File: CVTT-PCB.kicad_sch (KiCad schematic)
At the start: 66 parts, among them J1 SERVO1, J2 SERVO2, J3 LCD SCREEN, J4 LCD BUTTONS, J5 Conn_ARM_SWD_TagConnect_TC2030, J7 Barrel_Jack, P2 DC2, P5 DC1, P8 STEPPER, Q7 BSS138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

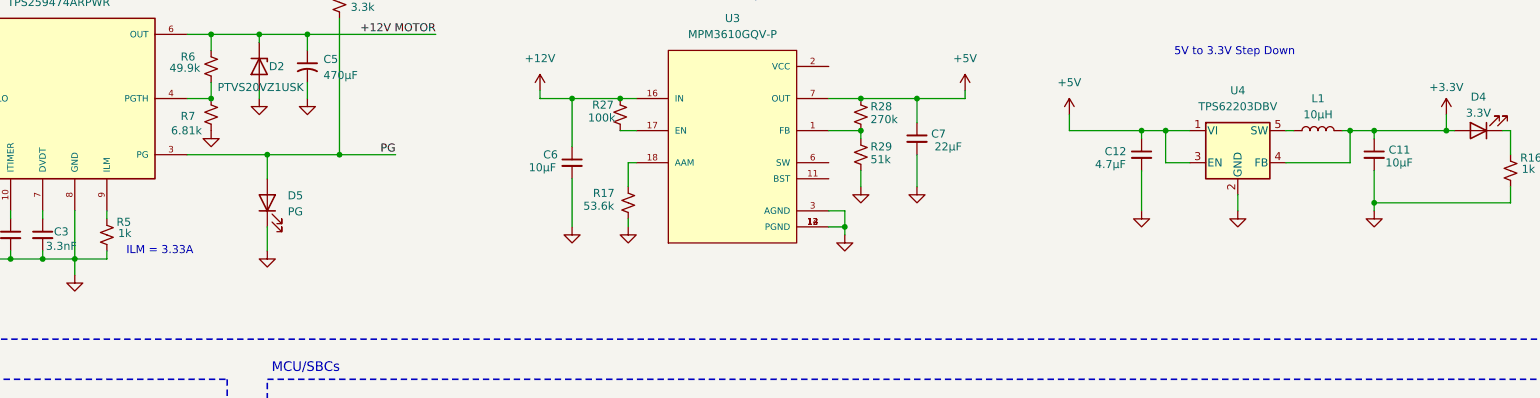
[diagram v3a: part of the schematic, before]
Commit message: reconfigure ILM for motor req
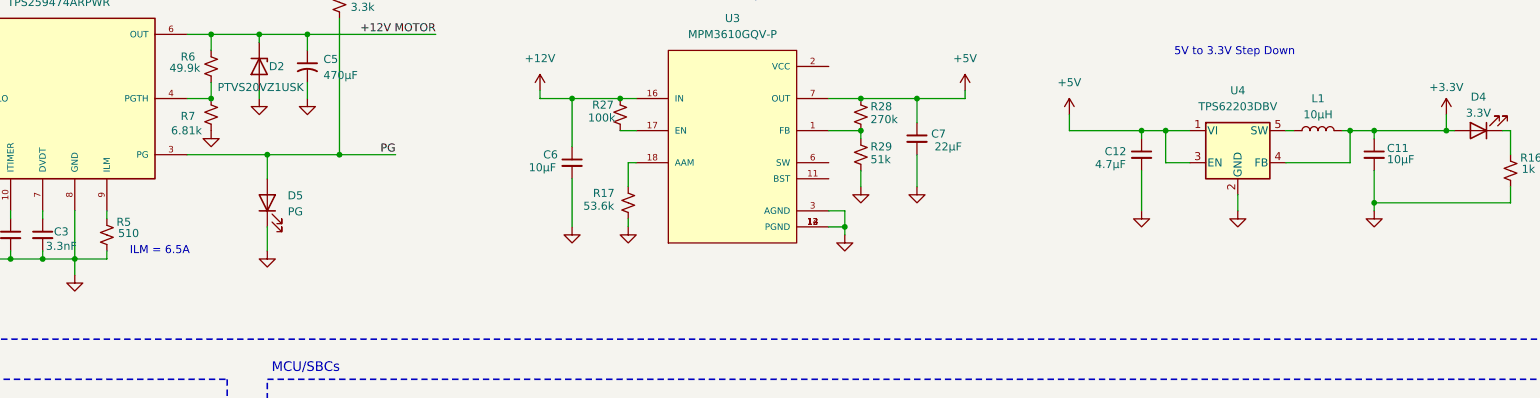
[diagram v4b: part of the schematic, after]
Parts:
- C11, C6: Manufacturer (none) -> Murata Electronics; Part Number (none) -> GRM188R61E106KA73D
- C12: Manufacturer (none) -> Samsung Electro-Mechanics; Part Number (none) -> CL10A475KO8NNNC
- C7: Manufacturer (none) -> Samsung Electro-Mechanics; Part Number (none) -> CL10A226MO7JZNC
- R17: Manufacturer (none) -> Vishay Dale; Part Number (none) -> CRCW060353K6FKEAC
- R5: value 1k -> 510; Manufacturer Vishay Dale -> YAGEO; Part Number RCS06031K00FKEA -> RC0603FR-07510RL
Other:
- note added: "ILM = 6.5A"
- note removed: "ILM = 3.33A"
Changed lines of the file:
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@@
 		)
 	)
-	(text "ILM = 3.33A"
+	(text "ILM = 6.5A"
 		(exclude_from_sim no)
 		(at 172.212 73.66 0)
@@
 			)
 		)
-		(property "Datasheet" ""
+		(property "Datasheet" "https://mm.digikey.com/Volume0/opasdata/d220001/medias/docus/2328/CL10A475KO8NNNC_Spec.pdf"
 			(at 327.66 58.42 0)
 			(effects
@@
 			)
 		)
-		(property "Description" ""
+		(property "Description" "CAP CER 4.7UF 16V X5R 0603"
 			(at 327.66 58.42 0)
 			(effects
@@
 			)
 		)
-		(property "Part Number" ""
+		(property "Part Number" "CL10A475KO8NNNC"
 			(at 327.66 58.42 0)
 			(effects
@@
 			)
 		)
-		(property "Manufacturer" ""
+		(property "Manufacturer" "Samsung Electro-Mechanics"
 			(at 327.66 58.42 0)
 			(effects
@@
 	)
 	(symbol
-		(lib_id "Device:C_Small")
-		(at 364.49 58.42 0)
-		(unit 1)
-		(exclude_from_sim no)
-		(in_bom yes)
-		(on_board yes)
-		(dnp no)
-		(property "Reference" "C11"
-			(at 366.776 57.658 0)
-			(effects
-				(font
-					(size 1.27 1.27)
-				)
-				(justify left)
-			)
-		)
-		(property "Value" "10µF"
-			(at 366.268 59.69 0)
-			(effects
-				(font
-					(size 1.27 1.27)
-				)
-				(justify left)
-			)
-		)
-		(property "Footprint" "Capacitor_SMD:C_0603_1608Metric_Pad1.08x0.95mm_HandSolder"
-			(at 364.49 58.42 0)
-			(effects
-				(font
-					(size 1.27 1.27)
-				)
-				(hide yes)
-			)
-		)
-		(property "Datasheet" ""
-			(at 364.49 58.42 0)
-			(effects
-				(font
-					(size 1.27 1.27)
-				)
-				(hide yes)
-			)
-		)
-		(property "Description" ""
-			(at 364.49 58.42 0)
-			(effects
-				(font
-					(size 1.27 1.27)
-				)
-				(hide yes)
-			)
-		)
-		(property "Part Number" ""
-			(at 364.49 58.42 0)
-			(effects
-				(font
-					(size 1.27 1.27)
-				)
-				(hide yes)
-			)
-		)
-		(property "Manufacturer" ""
-			(at 364.49 58.42 0)
-			(effects
-				(font
-					(size 1.27 1.27)
-				)
-				(hide yes)
-			)
-		)
-		(pin "1"
-		)
-		(pin "2"
-		)
-		(instances
-			(project "CVTT-PCB"
-				(path "/1cfd431a-19b0-4ea1-8526-1e2a0b724830"
-					(reference "C11")
-					(unit 1)
-				)
-			)
-		)
-	)
-	(symbol
 		(lib_id "power:+3.3V")
 		(at 71.12 115.57 0)
@@
 			)
 		)
-		(property "Datasheet" ""
+		(property "Datasheet" "https://mm.digikey.com/Volume0/opasdata/d220001/medias/docus/2139/CL10A226MO7JZNC_Spec.pdf"
 			(at 292.1 55.88 0)
 			(effects
@@
 			)
 		)
-		(property "Description" ""
+		(property "Description" "CAP CER 22UF 16V X5R 0603"
 			(at 292.1 55.88 0)
 			(effects
@@
 			)
 		)
-		(property "Part Number" ""
+		(property "Part Number" "CL10A226MO7JZNC"
 			(at 292.1 55.88 0)
 			(effects
@@
 			)
 		)
-		(property "Manufacturer" ""
+		(property "Manufacturer" "Samsung Electro-Mechanics"
 			(at 292.1 55.88 0)
 			(effects
@@
 			)
 		)
-		(property "Datasheet" ""
+		(property "Datasheet" "https://www.vishay.com/docs/28773/crcwce3.pdf"
 			(at 246.38 66.04 0)
 			(effects
@@
 			)
 		)
-		(property "Description" ""
+		(property "Description" "RES 53.6K OHM 1% 1/10W 0603"
 			(at 246.38 66.04 0)
 			(effects
@@
 			)
 		)
-		(property "Part Number" ""
+		(property "Part Number" "CRCW060353K6FKEAC"
 			(at 246.38 66.04 0)
 			(effects
@@
 			)
 		)
-		(property "Manufacturer" ""
+		(property "Manufacturer" "Vishay Dale"
 			(at 246.38 66.04 0)
 			(effects
@@
 			)
 		)
-		(property "Value" "1k"
+		(property "Value" "510"
 			(at 165.608 70.866 0)
 			(effects
@@
 			)
 		)
-		(property "Datasheet" "https://www.vishay.com/docs/20065/rcse3.pdf"
+		(property "Datasheet" "https://www.yageo.com/upload/media/product/products/datasheet/rchip/PYu-RC_Group_51_RoHS_L_12.pdf"
 			(at 163.83 71.12 0)
 			(effects
@@
 			)
 		)
-		(property "Description" "RES SMD 1K OHM 1% 1/4W 0603"
+		(property "Description" "RES 510 OHM 1% 1/10W 0603"
 			(at 163.83 71.12 0)
 			(effects
@@
 			)
 		)
-		(property "Part Number" "RCS06031K00FKEA"
+		(property "Part Number" "RC0603FR-07510RL"
 			(at 163.83 71.12 0)
 			(effects
@@
 			)
 		)
-		(property "Manufacturer" "Vishay Dale"
+		(property "Manufacturer" "YAGEO"
 			(at 163.83 71.12 0)
 			(effects
@@
 	)
 	(symbol
+		(lib_id "Device:C_Small")
+		(at 364.49 58.42 0)
+		(unit 1)
+		(exclude_from_sim no)
+		(in_bom yes)
+		(on_board yes)
+		(dnp no)
+		(property "Reference" "C11"
+			(at 366.522 57.404 0)
+			(effects
+				(font
+					(size 1.27 1.27)
+				)
+				(justify left)
+			)
+		)
+		(property "Value" "10µF"
+			(at 366.522 59.182 0)
+			(effects
+				(font
+					(size 1.27 1.27)
+				)
+				(justify left)
+			)
+		)
+		(property "Footprint" "Capacitor_SMD:C_0603_1608Metric_Pad1.08x0.95mm_HandSolder"
+			(at 364.49 58.42 0)
+			(effects
+				(font
+					(size 1.27 1.27)
+				)
+				(hide yes)
+			)
+		)
+		(property "Datasheet" "https://search.murata.co.jp/Ceramy/image/img/A01X/G101/ENG/GRM188R61E106KA73-01.pdf"
+			(at 364.49 58.42 0)
+			(effects
+				(font
+					(size 1.27 1.27)
+				)
+				(hide yes)
+			)
+		)
+		(property "Description" "CAP CER 10UF 25V X5R 0603"
+			(at 364.49 58.42 0)
+			(effects
+				(font
+					(size 1.27 1.27)
+				)
+				(hide yes)
+			)
+		)
+		(property "Part Number" "GRM188R61E106KA73D"
+			(at 364.49 58.42 0)
+			(effects
+				(font
+					(size 1.27 1.27)
+				)
+				(hide yes)
+			)
+		)
+		(property "Manufacturer" "Murata Electronics"
+			(at 364.49 58.42 0)
+			(effects
+				(font
+					(size 1.27 1.27)
+				)
+				(hide yes)
+			)
+		)
+		(pin "1"
+		)
+		(pin "2"
+		)
+		(instances
+			(project "CVTT-PCB"
+				(path "/1cfd431a-19b0-4ea1-8526-1e2a0b724830"
+					(reference "C11")
+					(unit 1)
+				)
+			)
+		)
+	)
+	(symbol
 		(lib_id "power:+5V")
 		(at 316.23 52.07 0)
@@
 			)
 		)
-		(property "Datasheet" ""
+		(property "Datasheet" "https://search.murata.co.jp/Ceramy/image/img/A01X/G101/ENG/GRM188R61E106KA73-01.pdf"
 			(at 237.49 59.69 0)
 			(effects
@@
 			)
 		)
-		(property "Description" ""
+		(property "Description" "CAP CER 10UF 25V X5R 0603"
 			(at 237.49 59.69 0)
 			(effects
@@
 			)
 		)
-		(property "Part Number" ""
+		(property "Part Number" "GRM188R61E106KA73D"
 			(at 237.49 59.69 0)
 			(effects
@@
 			)
 		)
-		(property "Manufacturer" ""
+		(property "Manufacturer" "Murata Electronics"
 			(at 237.49 59.69 0)
 			(effects

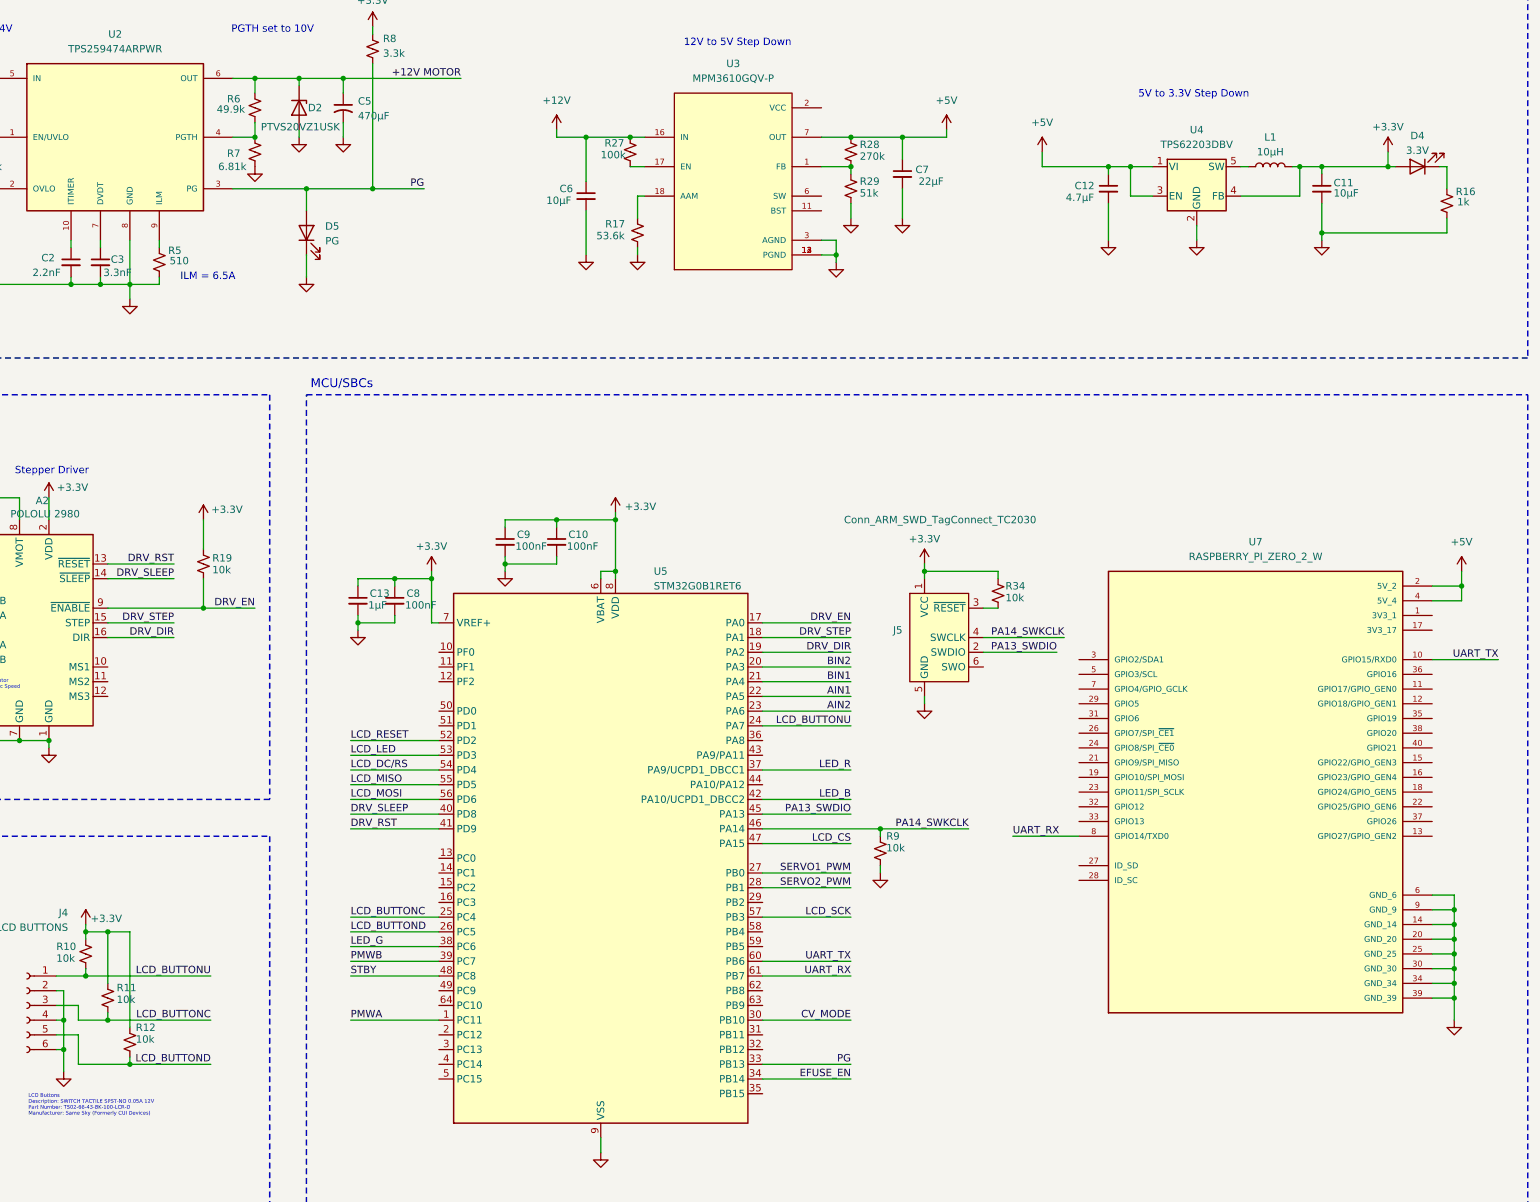
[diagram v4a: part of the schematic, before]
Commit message: resolve DRC errors
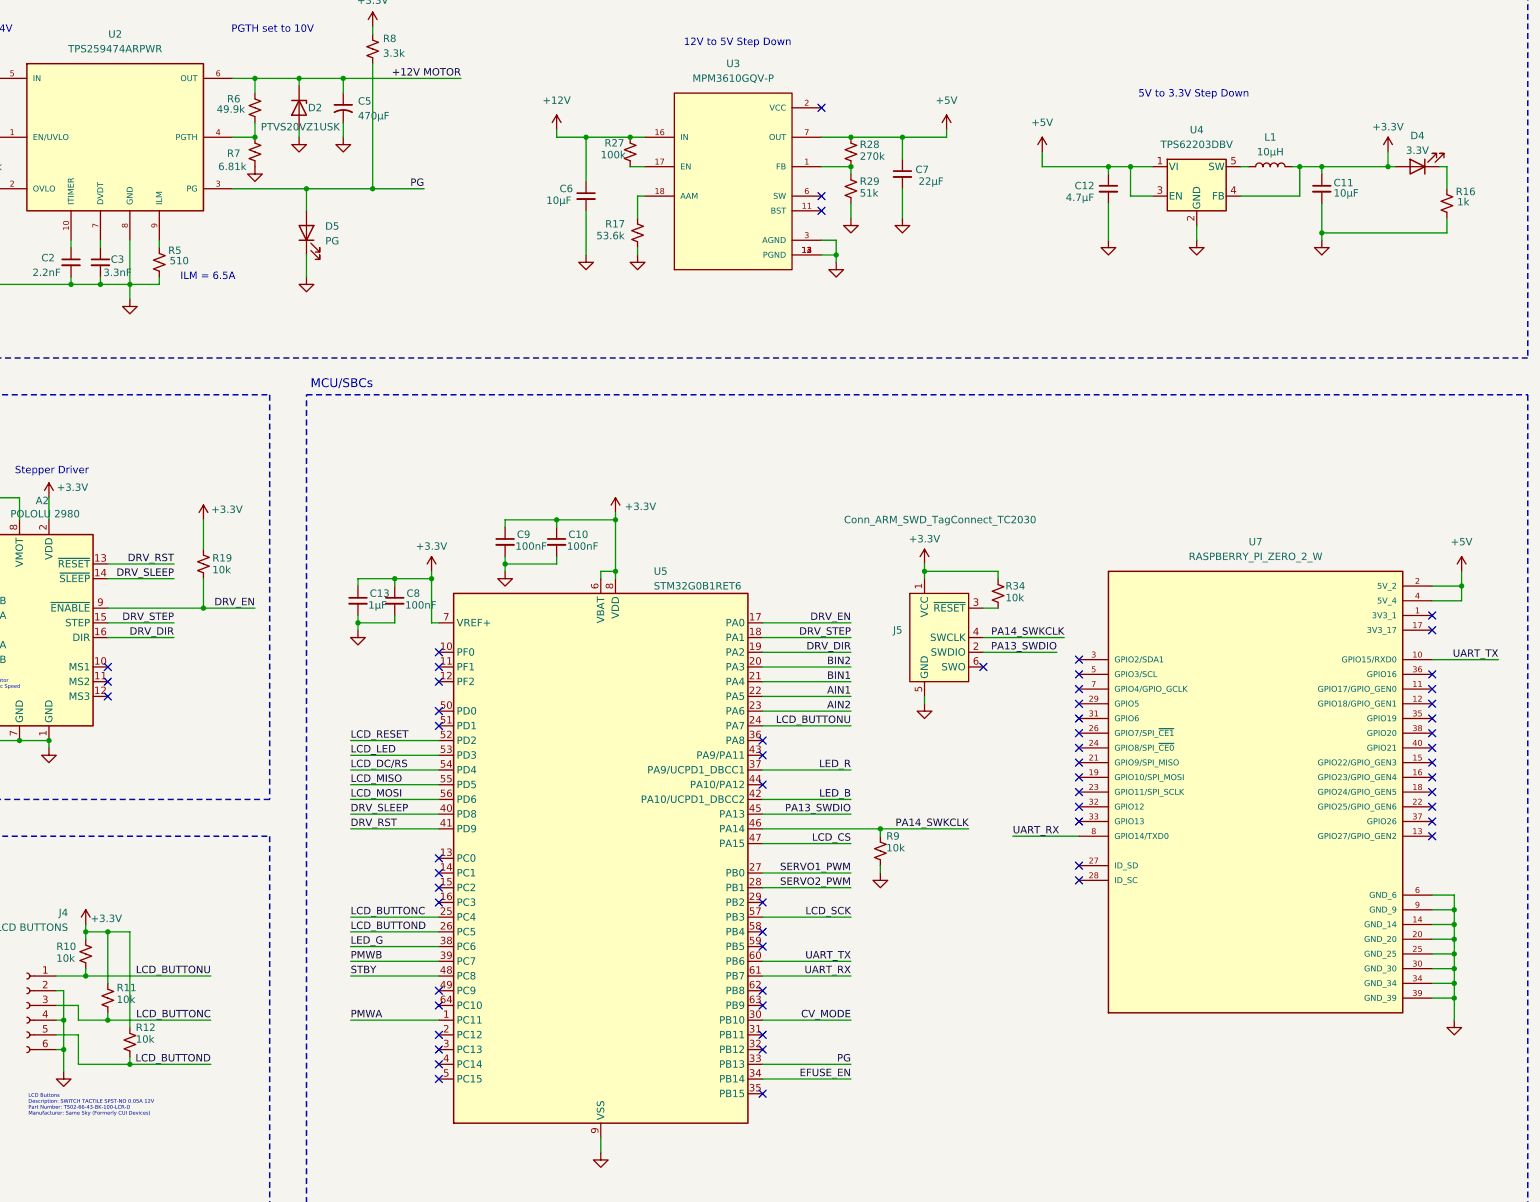
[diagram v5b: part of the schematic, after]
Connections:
- no-connect marks 0 -> 61
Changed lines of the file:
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@@
 		(color 0 0 0 0)
+	)
+	(no_connect
+		(at 212.09 212.09)
+	)
+	(no_connect
+		(at 322.58 142.24)
+	)
+	(no_connect
+		(at 267.97 156.21)
+	)
+	(no_connect
+		(at 322.58 144.78)
+	)
+	(no_connect
+		(at 154.94 140.97)
+	)
+	(no_connect
+		(at 267.97 207.01)
+	)
+	(no_connect
+		(at 383.54 154.94)
+	)
+	(no_connect
+		(at 322.58 165.1)
+	)
+	(no_connect
+		(at 322.58 157.48)
+	)
+	(no_connect
+		(at 322.58 139.7)
+	)
+	(no_connect
+		(at 154.94 143.51)
+	)
+	(no_connect
+		(at 278.13 62.23)
+	)
+	(no_connect
+		(at 154.94 146.05)
+	)
+	(no_connect
+		(at 267.97 214.63)
+	)
+	(no_connect
+		(at 322.58 152.4)
+	)
+	(no_connect
+		(at 267.97 153.67)
+	)
+	(no_connect
+		(at 322.58 177.8)
+	)
+	(no_connect
+		(at 322.58 147.32)
+	)
+	(no_connect
+		(at 212.09 204.47)
+	)
+	(no_connect
+		(at 212.09 173.99)
+	)
+	(no_connect
+		(at 306.07 140.97)
+	)
+	(no_connect
+		(at 267.97 199.39)
+	)
+	(no_connect
+		(at 267.97 204.47)
+	)
+	(no_connect
+		(at 383.54 132.08)
+	)
+	(no_connect
+		(at 383.54 142.24)
+	)
+	(no_connect
+		(at 383.54 160.02)
+	)
+	(no_connect
+		(at 212.09 196.85)
+	)
+	(no_connect
+		(at 267.97 196.85)
+	)
+	(no_connect
+		(at 212.09 179.07)
+	)
+	(no_connect
+		(at 212.09 207.01)
+	)
+	(no_connect
+		(at 267.97 181.61)
+	)
+	(no_connect
+		(at 383.54 134.62)
+	)
+	(no_connect
+		(at 212.09 140.97)
+	)
+	(no_connect
+		(at 212.09 151.13)
+	)
+	(no_connect
+		(at 278.13 44.45)
+	)
+	(no_connect
+		(at 212.09 199.39)
+	)
+	(no_connect
+		(at 322.58 167.64)
+	)
+	(no_connect
+		(at 267.97 161.29)
+	)
+	(no_connect
+		(at 383.54 144.78)
+	)
+	(no_connect
+		(at 212.09 138.43)
+	)
+	(no_connect
+		(at 383.54 152.4)
+	)
+	(no_connect
+		(at 278.13 59.69)
+	)
+	(no_connect
+		(at 212.09 209.55)
+	)
+	(no_connect
+		(at 383.54 162.56)
+	)
+	(no_connect
+		(at 267.97 186.69)
+	)
+	(no_connect
+		(at 383.54 149.86)
+	)
+	(no_connect
+		(at 383.54 167.64)
+	)
+	(no_connect
+		(at 383.54 147.32)
+	)
+	(no_connect
+		(at 322.58 175.26)
+	)
+	(no_connect
+		(at 212.09 181.61)
+	)
+	(no_connect
+		(at 212.09 176.53)
+	)
+	(no_connect
+		(at 383.54 165.1)
+	)
+	(no_connect
+		(at 267.97 189.23)
+	)
+	(no_connect
+		(at 322.58 160.02)
+	)
+	(no_connect
+		(at 212.09 143.51)
+	)
+	(no_connect
+		(at 383.54 157.48)
+	)
+	(no_connect
+		(at 322.58 154.94)
+	)
+	(no_connect
+		(at 383.54 170.18)
+	)
+	(no_connect
+		(at 322.58 149.86)
+	)
+	(no_connect
+		(at 322.58 162.56)
+	)
+	(no_connect
+		(at 212.09 148.59)
 	)
 	(wire

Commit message: final check before gerbers
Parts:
- U7: value RASPBERRY_PI_ZERO_2_W -> RASPBERRY PI ZERO 2 W
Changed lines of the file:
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@@
 			)
 		)
-		(property "Value" "RASPBERRY_PI_ZERO_2_W"
+		(property "Value" "RASPBERRY PI ZERO 2 W"
 			(at 353.06 121.92 0)
 			(effects

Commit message: update sch info
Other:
- note added: "DCs Description: ProFast 12V 5900RPM Fast Gearmotor Part Number: JS19198 Manufacturer: ProFast"
- note removed: "DCs Description: Part Number: Manufacturer:"
- moved on the sheet: A2, C4, P8, R19

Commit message: edit sch
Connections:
- net +12V: now also C1.1, R1.1, R3.1, R31.1, U2.5 (IN)
- net PMWA renamed PWMA
- net PMWB renamed PWMB
- new net: D3.1 (K), R15.1
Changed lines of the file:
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@@
 	)
 	(junction
-		(at 69.85 39.37)
+		(at 151.13 194.31)
 		(diameter 0)
 		(color 0 0 0 0)
 	)
 	(junction
-		(at 151.13 194.31)
+		(at 283.21 54.61)
 		(diameter 0)
 		(color 0 0 0 0)
 	)
 	(junction
-		(at 283.21 54.61)
+		(at 74.93 39.37)
 		(diameter 0)
 		(color 0 0 0 0)
@@
 	)
 	(junction
+		(at 44.45 34.29)
+		(diameter 0)
+		(color 0 0 0 0)
+	)
+	(junction
 		(at 120.65 74.93)
 		(diameter 0)
@@
 	)
 	(junction
-		(at 74.93 39.37)
-		(diameter 0)
-		(color 0 0 0 0)
-	)
-	(junction
 		(at 105.41 110.49)
 		(diameter 0)
@@
 	(wire
 		(pts
+			(xy 44.45 34.29) (xy 44.45 39.37)
+		)
+		(stroke
+			(width 0)
+			(type default)
+		)
+	)
+	(wire
+		(pts
 			(xy 267.97 163.83) (xy 283.21 163.83)
 		)
@@
 	(wire
 		(pts
-			(xy 44.45 31.75) (xy 44.45 39.37)
+			(xy 44.45 30.48) (xy 44.45 34.29)
 		)
 		(stroke
@@
 	(wire
 		(pts
+			(xy 44.45 34.29) (xy 74.93 34.29)
+		)
+		(stroke
+			(width 0)
+			(type default)
+		)
+	)
+	(wire
+		(pts
 			(xy 151.13 193.04) (xy 151.13 194.31)
 		)
@@
 	(wire
 		(pts
+			(xy 74.93 34.29) (xy 74.93 39.37)
+		)
+		(stroke
+			(width 0)
+			(type default)
+		)
+	)
+	(wire
+		(pts
 			(xy 232.41 115.57) (xy 232.41 116.84)
 		)
@@
 	(wire
 		(pts
-			(xy 69.85 39.37) (xy 74.93 39.37)
-		)
-		(stroke
-			(width 0)
-			(type default)
-		)
-	)
-	(wire
-		(pts
 			(xy 386.08 54.61) (xy 386.08 58.42)
 		)
@@
 		)
 	)
-	(label "PMWB"
+	(label "PWMB"
 		(at 36.83 137.16 0)
 		(effects
@@
 		)
 	)
-	(label "PMWA"
+	(label "PWMA"
 		(at 36.83 134.62 0)
 		(effects
@@
 		)
 	)
-	(label "PMWB"
+	(label "PWMB"
 		(at 196.85 191.77 0)
 		(effects
@@
 		)
 	)
-	(label "PMWA"
+	(label "PWMA"
 		(at 196.85 201.93 0)
 		(effects
@@
 		(dnp no)
 		(property "Reference" "D3"
-			(at 62.23 33.782 0)
+			(at 62.23 36.322 0)
 			(effects
 				(font
@@
 		)
 		(property "Value" "12V"
-			(at 62.23 36.322 0)
+			(at 62.23 42.164 0)
 			(effects
 				(font
@@
 	(symbol
 		(lib_id "power:+12V")
-		(at 44.45 31.75 0)
+		(at 44.45 30.48 0)
 		(unit 1)
 		(exclude_from_sim no)
@@
 		(dnp no)
 		(property "Reference" "#PWR017"
-			(at 44.45 35.56 0)
+			(at 44.45 34.29 0)
 			(effects
 				(font
@@
 		)
 		(property "Value" "+12V"
-			(at 43.942 27.686 0)
+			(at 43.942 26.416 0)
 			(effects
 				(font
@@
 		)
 		(property "Footprint" ""
-			(at 44.45 31.75 0)
+			(at 44.45 30.48 0)
 			(effects
 				(font
@@
 		)
 		(property "Datasheet" ""
-			(at 44.45 31.75 0)
+			(at 44.45 30.48 0)
 			(effects
 				(font
@@
 		)
 		(property "Description" "Power symbol creates a global label with name \"+12V\""
-			(at 44.45 31.75 0)
+			(at 44.45 30.48 0)
 			(effects
 				(font
